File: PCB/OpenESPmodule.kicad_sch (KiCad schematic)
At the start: 24 parts, among them J1 PINHD_1x15_Female, J3 USB_C_Receptacle_USB2.0_16P, SW1 SW_Push, SW2 SW_Push, U1 ESP32-C3-WROOM-02, U2 SPX3819M5-L-3-3, U3 MCP9700Ax-HLT, U4 4N28, U5 XL1509-3.3

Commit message: tri
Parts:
- added BT1: Battery_Cell, Battery:BatteryHolder_Keystone_1060_1x2032, symbol Device:Battery_Cell
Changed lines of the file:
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@@
+	)
+	(symbol
+		(lib_id "Device:Battery_Cell")
+		(at 168.91 116.84 0)
+		(unit 1)
+		(exclude_from_sim no)
+		(in_bom yes)
+		(on_board yes)
+		(dnp no)
+		(fields_autoplaced yes)
+		(property "Reference" "BT1"
+			(at 172.72 113.7284 0)
+			(effects
+				(font
+					(size 1.27 1.27)
+				)
+				(justify left)
+			)
+		)
+		(property "Value" "Battery_Cell"
+			(at 172.72 116.2684 0)
+			(effects
+				(font
+					(size 1.27 1.27)
+				)
+				(justify left)
+			)
+		)
+		(property "Footprint" "Battery:BatteryHolder_Keystone_1060_1x2032"
+			(at 168.91 115.316 90)
+			(effects
+				(font
+					(size 1.27 1.27)
+				)
+				(hide yes)
+			)
+		)
+		(property "Datasheet" "~"
+			(at 168.91 115.316 90)
+			(effects
+				(font
+					(size 1.27 1.27)
+				)
+				(hide yes)
+			)
+		)
+		(property "Description" "Single-cell battery"
+			(at 168.91 116.84 0)
+			(effects
+				(font
+					(size 1.27 1.27)
+				)
+				(hide yes)
+			)
+		)
+		(pin "2"
+		)
+		(pin "1"
+		)
+		(instances
+			(project ""
+				(path "/a6ab6f10-55f4-4100-8917-84055be0855c"
+					(reference "BT1")
+					(unit 1)
+				)
+			)
+		)
 	)
 	(symbol

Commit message: ammelioration de la carte + Update README
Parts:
- removed D1: LED, LED_THT:LED_VCCLite_5381H5_6.35x6.35mm, symbol PCM_SL_Devices:LED
- removed U5: XL1509-3.3, Package_SO:SOIC-8_3.9x4.9mm_P1.27mm, symbol Regulator_Switching:XL1509-3.3
- added C10: 4.7u, symbol Device:C
- added C11: 10u, symbol Device:C
- added D1: IR26-21C_L110_TR8, LED_SMD:LED_1206_3216Metric_Pad1.42x1.75mm_HandSolder, symbol LED:IR26-21C_L110_TR8
- added L1: 2.2u, symbol Device:L
- added R6, R7: 100k, symbol Device:R
- added U6: ST1S12XX, Package_TO_SOT_SMD:TSOT-23-5, symbol Regulator_Switching:ST1S12XX
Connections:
- net +3.3V: now also D1.2 (A)
- net Earth: now also BT1.2 (-), C10.2, C11.2, R6.2, U6.2 (GND)
- net at R3.1: now also D1.1 (K)
- net at BT1.1 (+): now also C10.1, U6.1 (EN), U6.4 (V_{IN})
- new net: R6.1, R7.1, U6.5 (FB/V_{O})
- new net: C11.1, L1.2, R7.2
- new net: L1.1, U6.3 (SW)
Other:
- moved on the sheet: BT1

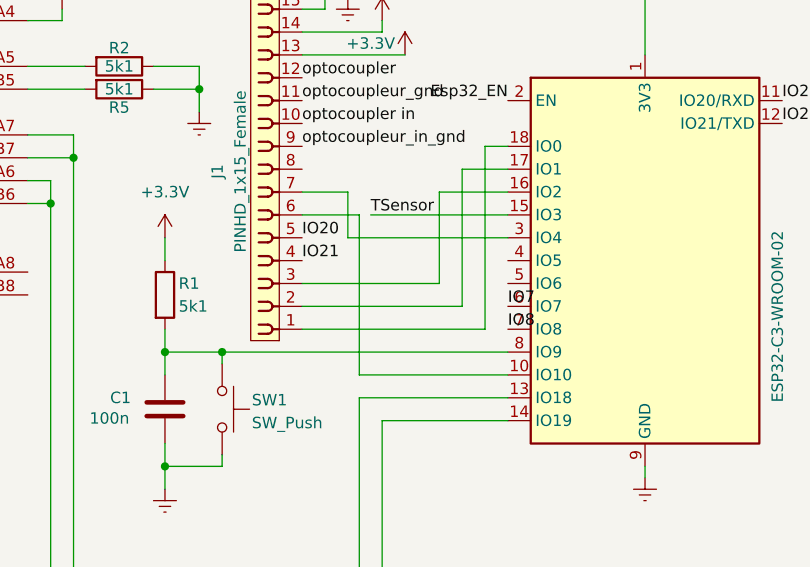
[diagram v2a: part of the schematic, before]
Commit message: Add power managment
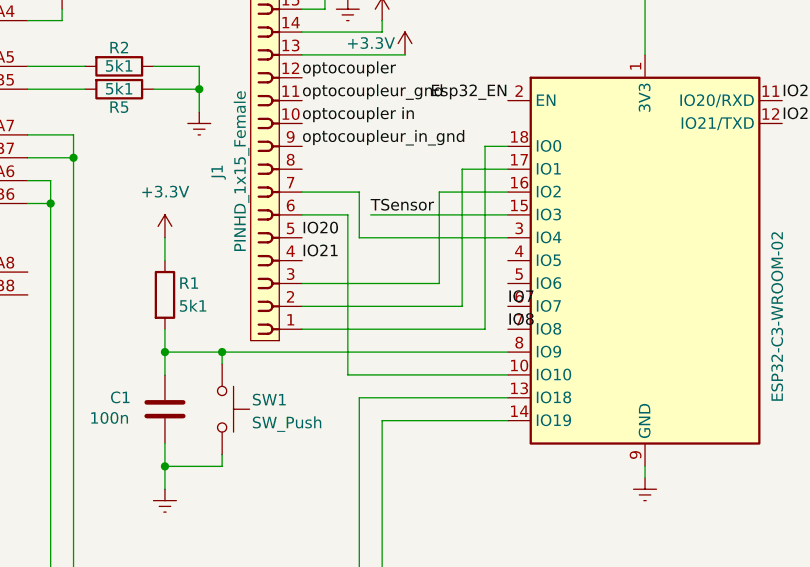
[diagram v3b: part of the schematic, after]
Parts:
- C10: footprint (none) -> Capacitor_SMD:C_0201_0603Metric
- L1: footprint (none) -> Inductor_SMD:L_0201_0603Metric
- R6, R7: footprint (none) -> Resistor_SMD:R_0201_0603Metric
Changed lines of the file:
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@@
 	(wire
 		(pts
-			(xy 101.6 163.83) (xy 85.09 163.83)
+			(xy 101.6 163.83) (xy 83.82 163.83)
 		)
 		(stroke
 			(width 0)
 			(type default)
+			(color 0 0 255 1)
 		)
 	)
@@
 	(wire
 		(pts
-			(xy 101.6 148.59) (xy 83.82 148.59)
+			(xy 101.6 148.59) (xy 85.09 148.59)
 		)
 		(stroke
 			(width 0)
 			(type default)
+			(color 0 0 255 1)
 		)
 	)
@@
 	(wire
 		(pts
-			(xy 78.74 143.51) (xy 83.82 143.51)
+			(xy 78.74 143.51) (xy 85.09 143.51)
 		)
 		(stroke
 			(width 0)
 			(type default)
+			(color 0 0 255 1)
 		)
 	)
@@
 	(wire
 		(pts
-			(xy 85.09 163.83) (xy 85.09 146.05)
+			(xy 83.82 163.83) (xy 83.82 146.05)
 		)
 		(stroke
 			(width 0)
 			(type default)
+			(color 0 0 255 1)
 		)
 	)
@@
 			(width 0)
 			(type default)
+			(color 0 0 255 1)
 		)
 	)
@@
 	(wire
 		(pts
-			(xy 85.09 146.05) (xy 78.74 146.05)
+			(xy 83.82 146.05) (xy 78.74 146.05)
 		)
 		(stroke
 			(width 0)
 			(type default)
+			(color 0 0 255 1)
 		)
 	)
@@
 	(wire
 		(pts
-			(xy 83.82 148.59) (xy 83.82 143.51)
+			(xy 85.09 148.59) (xy 85.09 143.51)
 		)
 		(stroke
 			(width 0)
 			(type default)
+			(color 0 0 255 1)
 		)
 	)
@@
 			)
 		)
-		(property "Footprint" ""
+		(property "Footprint" "Capacitor_SMD:C_0201_0603Metric"
 			(at 159.7152 124.46 0)
 			(effects
@@
 			)
 		)
-		(property "Footprint" ""
+		(property "Footprint" "Resistor_SMD:R_0201_0603Metric"
 			(at 184.15 118.618 90)
 			(effects
@@
 			)
 		)
-		(property "Footprint" ""
+		(property "Footprint" "Resistor_SMD:R_0201_0603Metric"
 			(at 178.562 120.65 90)
 			(effects
@@
 			)
 		)
-		(property "Footprint" ""
+		(property "Footprint" "Inductor_SMD:L_0201_0603Metric"
 			(at 184.15 111.76 0)
 			(effects

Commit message: Update
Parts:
- C11: footprint (none) -> Capacitor_SMD:C_0201_0603Metric
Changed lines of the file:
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@@
 	(title_block
 		(title "Open Esp32")
-		(rev "0.1")
+		(rev "0.2")
 		(comment 1 "Licence : LOC (loc.zyglonk.fr)")
 	)
@@
 	(wire
 		(pts
+			(xy 101.6 129.54) (xy 101.6 133.35)
+		)
+		(stroke
+			(width 0)
+			(type default)
+		)
+	)
+	(wire
+		(pts
 			(xy 87.63 125.73) (xy 78.74 125.73)
 		)
@@
 	)
 	(label "Esp32_EN"
-		(at 101.6 133.35 180)
+		(at 101.6 129.54 180)
 		(effects
 			(font
@@
 			)
 		)
-		(property "Footprint" ""
+		(property "Footprint" "Capacitor_SMD:C_0201_0603Metric"
 			(at 188.9252 124.46 0)
 			(effects
@@
 		(dnp no)
 		(property "Reference" "R6"
-			(at 176.276 120.396 0)
+			(at 180.34 121.92 90)
 			(effects
 				(font
@@
 		)
 		(property "Value" "100k"
-			(at 174.498 121.92 0)
+			(at 178.308 123.952 90)
 			(effects
 				(font
